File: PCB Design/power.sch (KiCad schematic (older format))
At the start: 19 parts, among them CON2 BARREL_JACK, P1 Power Sel, U1 3.3VREG

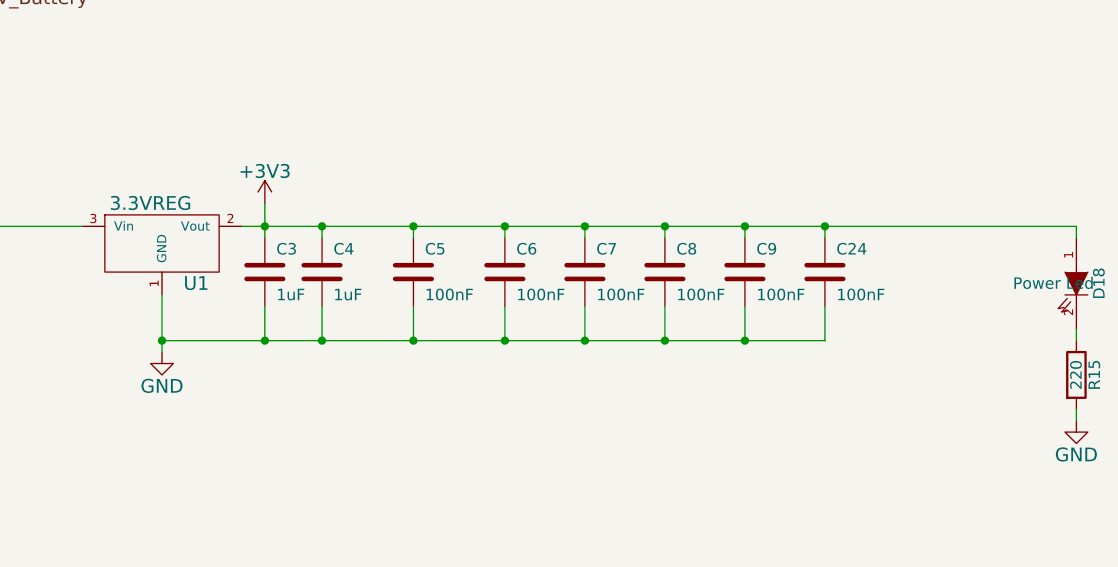
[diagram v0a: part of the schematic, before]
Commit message: Changed all via sizes, changed layout, changed jack footprint to original
Signed-off-by: Kolijn Wolfaardt <kolijn.wolfaardt@gmail.com>
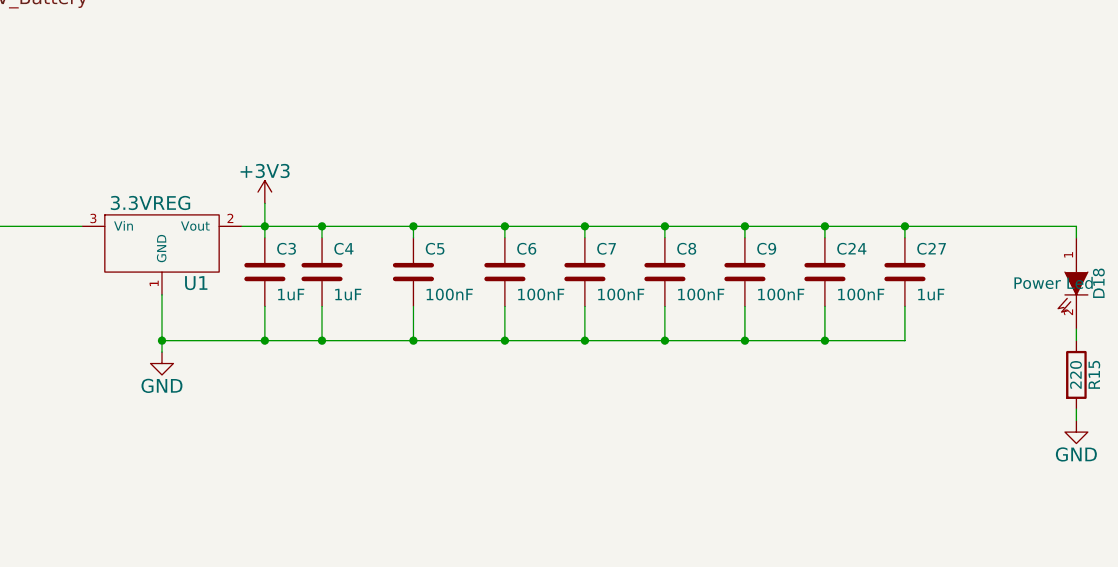
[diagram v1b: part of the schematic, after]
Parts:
- added C27: 1uF, Capacitors_SMD:C_1206, symbol C
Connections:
- net +3V3: now also C27.1
- net GND: now also C27.2
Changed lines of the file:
@@
 $EndDescr
 $Comp
-L +3V3 #PWR01
+L +3V3 #PWR5
 U 1 1 551253EA
 P 6600 2250
-F 0 "#PWR01" H 6600 2100 60  0001 C CNN
+F 0 "#PWR5" H 6600 2100 60  0001 C CNN
 F 1 "+3V3" H 6600 2390 60  0000 C CNN
 F 2 "" H 6600 2250 60  0000 C CNN
@@
 $EndComp
 $Comp
-L GND #PWR02
+L GND #PWR6
 U 1 1 551253F0
 P 6600 2400
-F 0 "#PWR02" H 6600 2150 60  0001 C CNN
+F 0 "#PWR6" H 6600 2150 60  0001 C CNN
 F 1 "GND" H 6600 2250 60  0000 C CNN
 F 2 "" H 6600 2400 60  0000 C CNN
@@
 $EndComp
 $Comp
-L +3V3 #PWR03
+L +3V3 #PWR7
 U 1 1 551258E1
 P 6600 3800
-F 0 "#PWR03" H 6600 3650 60  0001 C CNN
+F 0 "#PWR7" H 6600 3650 60  0001 C CNN
 F 1 "+3V3" H 6600 3940 60  0000 C CNN
 F 2 "" H 6600 3800 60  0000 C CNN
@@
 	6600 3800 6600 3950
 $Comp
-L GND #PWR04
+L GND #PWR4
 U 1 1 55125915
 P 6150 4450
-F 0 "#PWR04" H 6150 4200 60  0001 C CNN
+F 0 "#PWR4" H 6150 4200 60  0001 C CNN
 F 1 "GND" H 6150 4300 60  0000 C CNN
 F 2 "" H 6150 4450 60  0000 C CNN
@@
 $EndComp
 $Comp
-L GND #PWR05
+L GND #PWR2
 U 1 1 55125A29
 P 4300 5100
-F 0 "#PWR05" H 4300 4850 60  0001 C CNN
+F 0 "#PWR2" H 4300 4850 60  0001 C CNN
 F 1 "GND" H 4300 4950 60  0000 C CNN
 F 2 "" H 4300 5100 60  0000 C CNN
@@
 $EndComp
 Wire Wire Line
-	6150 4400 9050 4400
+	6150 4400 9400 4400
 Wire Wire Line
 	6600 4250 6600 4400
@@
 Connection ~ 8350 3900
 $Comp
-L GND #PWR06
+L GND #PWR1
 U 1 1 551264A9
 P 2950 3250
-F 0 "#PWR06" H 2950 3000 60  0001 C CNN
+F 0 "#PWR1" H 2950 3000 60  0001 C CNN
 F 1 "GND" H 2950 3100 60  0000 C CNN
 F 2 "" H 2950 3250 60  0000 C CNN
@@
 Connection ~ 4450 2900
 $Comp
-L GND #PWR07
+L GND #PWR3
 U 1 1 5513CAE7
 P 4600 3350
-F 0 "#PWR07" H 4600 3100 60  0001 C CNN
+F 0 "#PWR3" H 4600 3100 60  0001 C CNN
 F 1 "GND" H 4600 3200 60  0000 C CNN
 F 2 "" H 4600 3350 60  0000 C CNN
@@
 $EndComp
 $Comp
-L GND #PWR08
+L GND #PWR8
 U 1 1 551841D4
 P 10150 4750
-F 0 "#PWR08" H 10150 4500 60  0001 C CNN
+F 0 "#PWR8" H 10150 4500 60  0001 C CNN
 F 1 "GND" H 10150 4600 60  0000 C CNN
 F 2 "" H 10150 4750 60  0000 C CNN
@@
 	9050 4400 9050 4250
 Connection ~ 8700 4400
+$Comp
+L C C27
+U 1 1 554B20EC
+P 9400 4100
+F 0 "C27" H 9450 4200 50  0000 L CNN
+F 1 "1uF" H 9450 4000 50  0000 L CNN
+F 2 "Capacitors_SMD:C_1206" H 9438 3950 30  0001 C CNN
+F 3 "" H 9400 4100 60  0000 C CNN
+	1    9400 4100
+	1    0    0    -1
+$EndComp
+Wire Wire Line
+	9400 4400 9400 4250
+Connection ~ 9050 4400
+Wire Wire Line
+	9400 3900 9400 3950
+Connection ~ 9400 3900
 $EndSCHEMATC
